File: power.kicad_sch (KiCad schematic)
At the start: 28 parts, among them U4 INA3221AIRGV, U6 TI LMR54410DBV

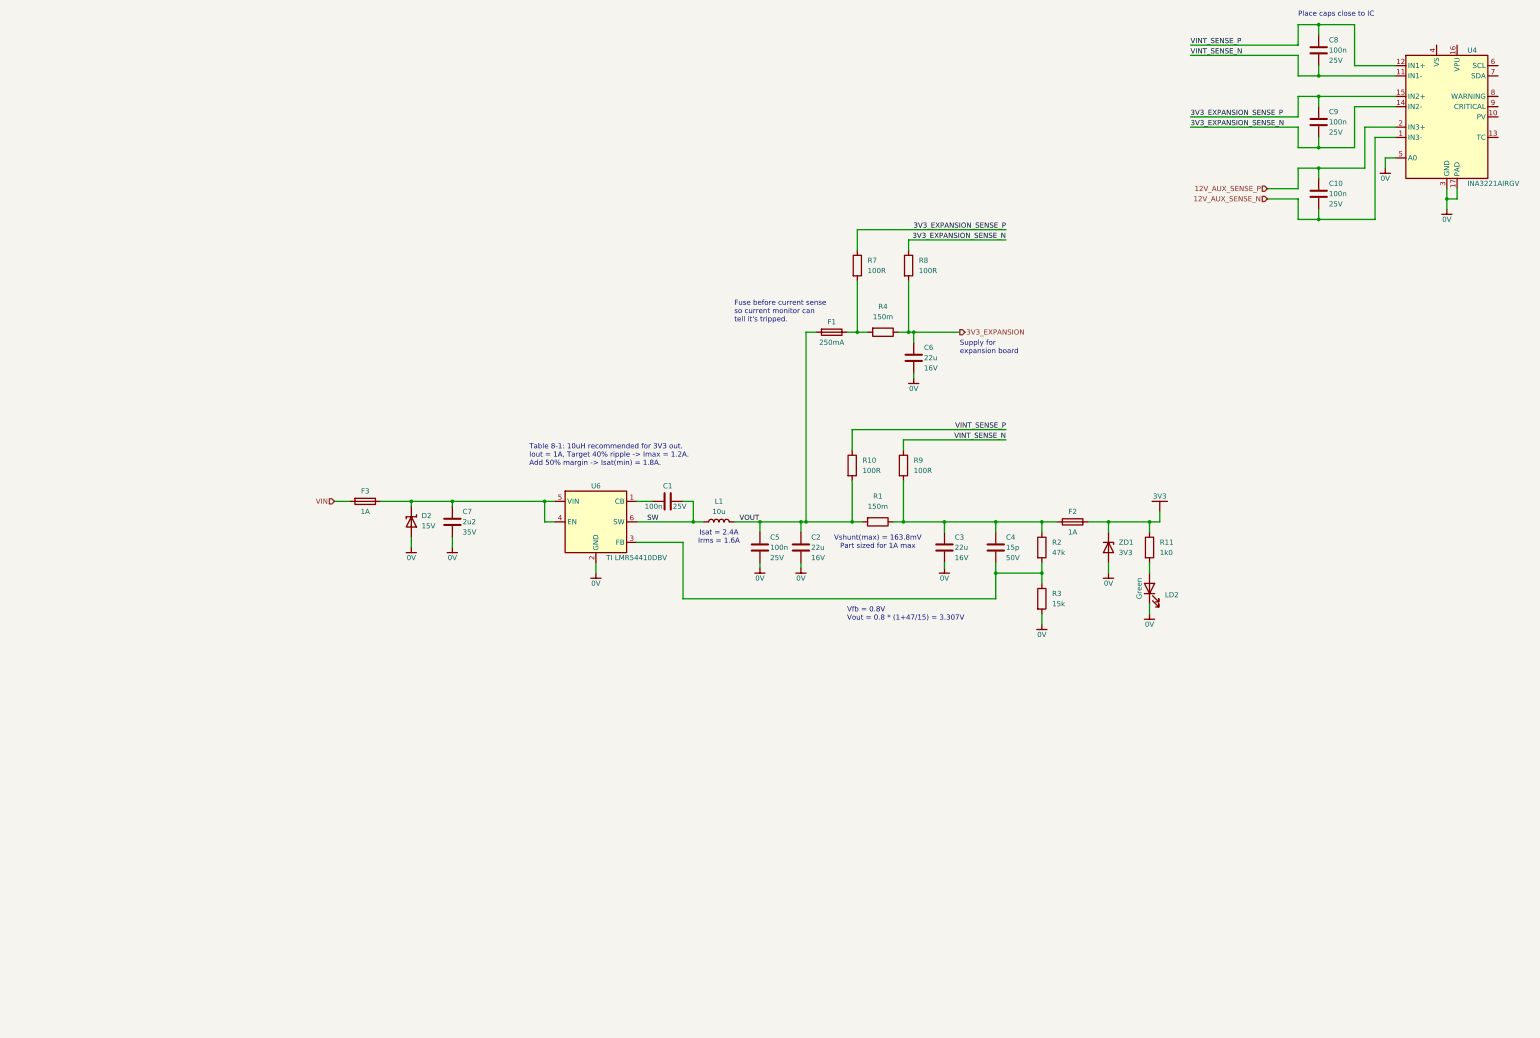
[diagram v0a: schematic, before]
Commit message: added ethernet phy
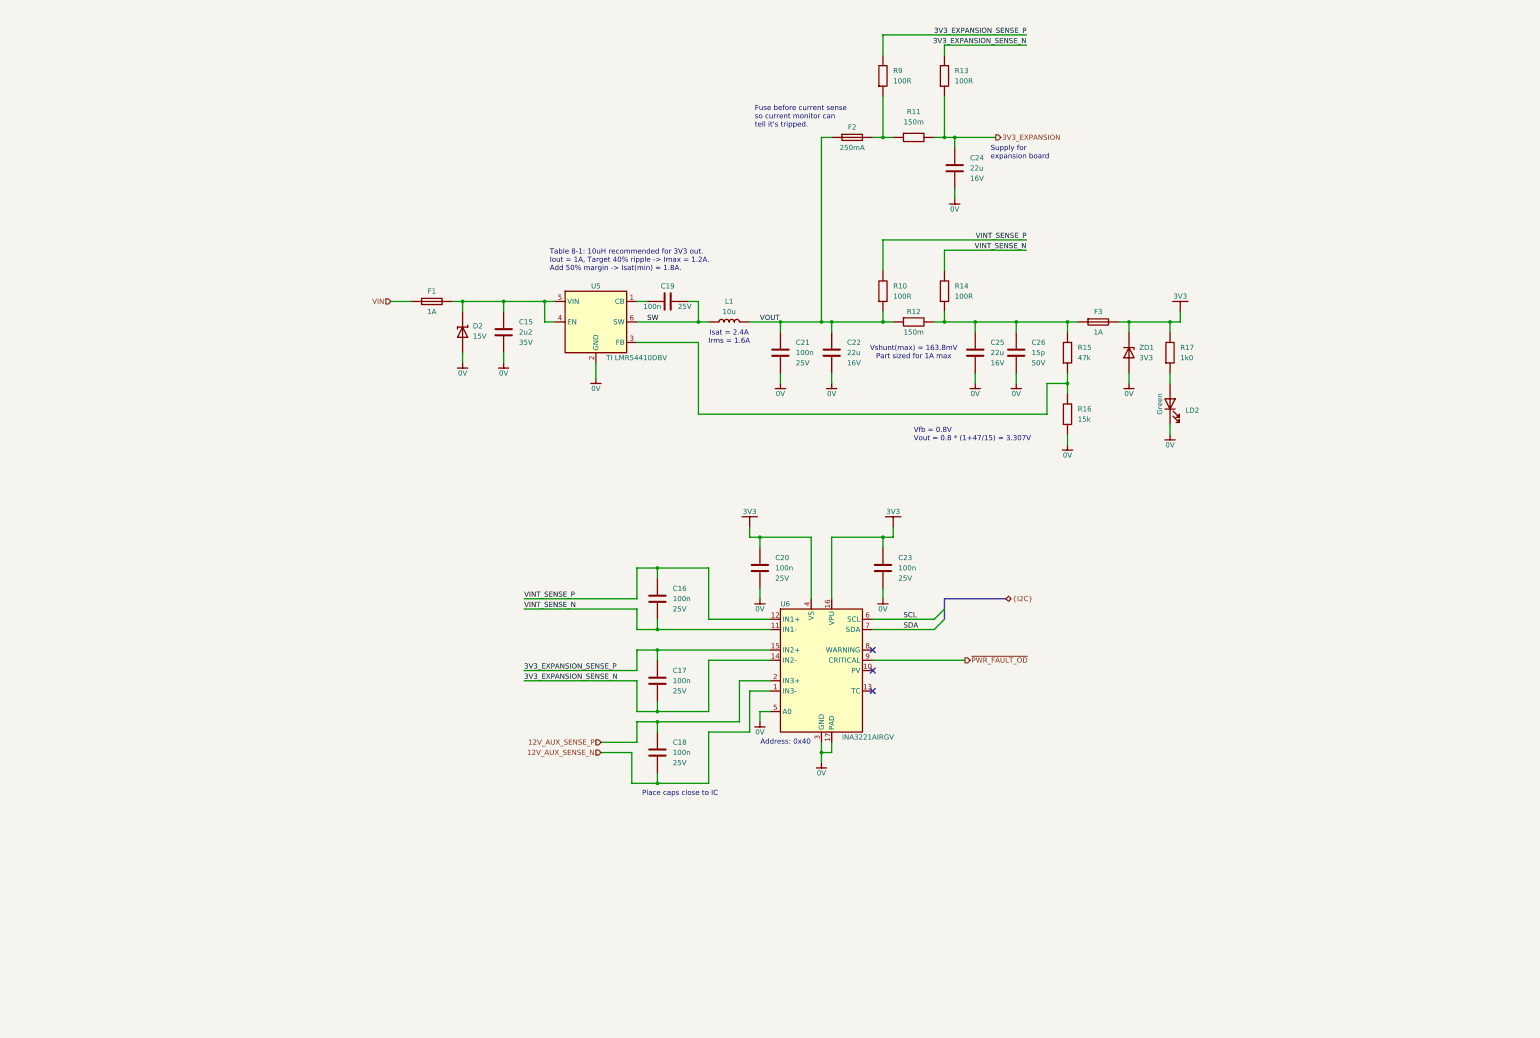
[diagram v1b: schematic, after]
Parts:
- removed C1: 100n, Capacitor_WUT:C_0402_1005Metric, symbol aaa_capacitor_auto_wut:Yageo CC0402KRX7R8BB104
- removed D2: 15V, Diode_SMD:D_SOD-523, symbol tvs_zener_auto_wut:nexperia PESD15VS1UB,115
- added C19, C20, C23: 100n, Capacitor_WUT:C_0402_1005Metric, symbol aaa_capacitor_auto_wut:Yageo CC0402KRX7R8BB104
- added D2: 15V, Diode_SMD:D_SOD-323, symbol tvs_zener_auto_wut:Bourns CDSOD323-T15S
- renumbered C7 to C15, C8 to C16, C9 to C17, C10 to C18, C5 to C21, C2 to C22, C6 to C24, C3 to C25, C4 to C26, F3 to F1, F1 to F2, F2 to F3, R4 to R11, R1 to R12, R8 to R13, R9 to R14, R2 to R15, R3 to R16, R11 to R17, R7 to R9, U6 to U5, U4 to U6
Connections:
- net 0V: now also C26.2, C20.2, C23.2, D2.2 (A)
- net 3V3: now also U6.16 (VPU), U6.4 (VS), C20.1, C23.1
- net SW: now also C19.1
- net SCL: now reaches U6.6 (SCL)
- net SDA: now reaches U6.7 (SDA)
- net ~{PWR_FAULT_OD}: now reaches U6.9 (CRITICAL)
- net at C15.1, F1.2, U5.4 (EN)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: now also D2.1 (K)
- net at U5.1 (CB): now also C19.2
- net at R15.2, R16.1, U5.3 (FB): no longer C26.2
- no-connect marks 0 -> 3
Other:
- note added: "Address: 0x40"
- moved on the sheet: C15, C16, C17, C18, C21, C22, C24, C25, C26, F1, F2, F3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
